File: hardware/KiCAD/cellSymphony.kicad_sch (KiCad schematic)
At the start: 11 parts, among them SW1 RotaryEncoder_Switch, SW2 RotaryEncoder_Switch, SW3 RotaryEncoder_Switch, SW4 RotaryEncoder_Switch, SW5 RotaryEncoder_Switch, U1 Raspberry Zero 2 W

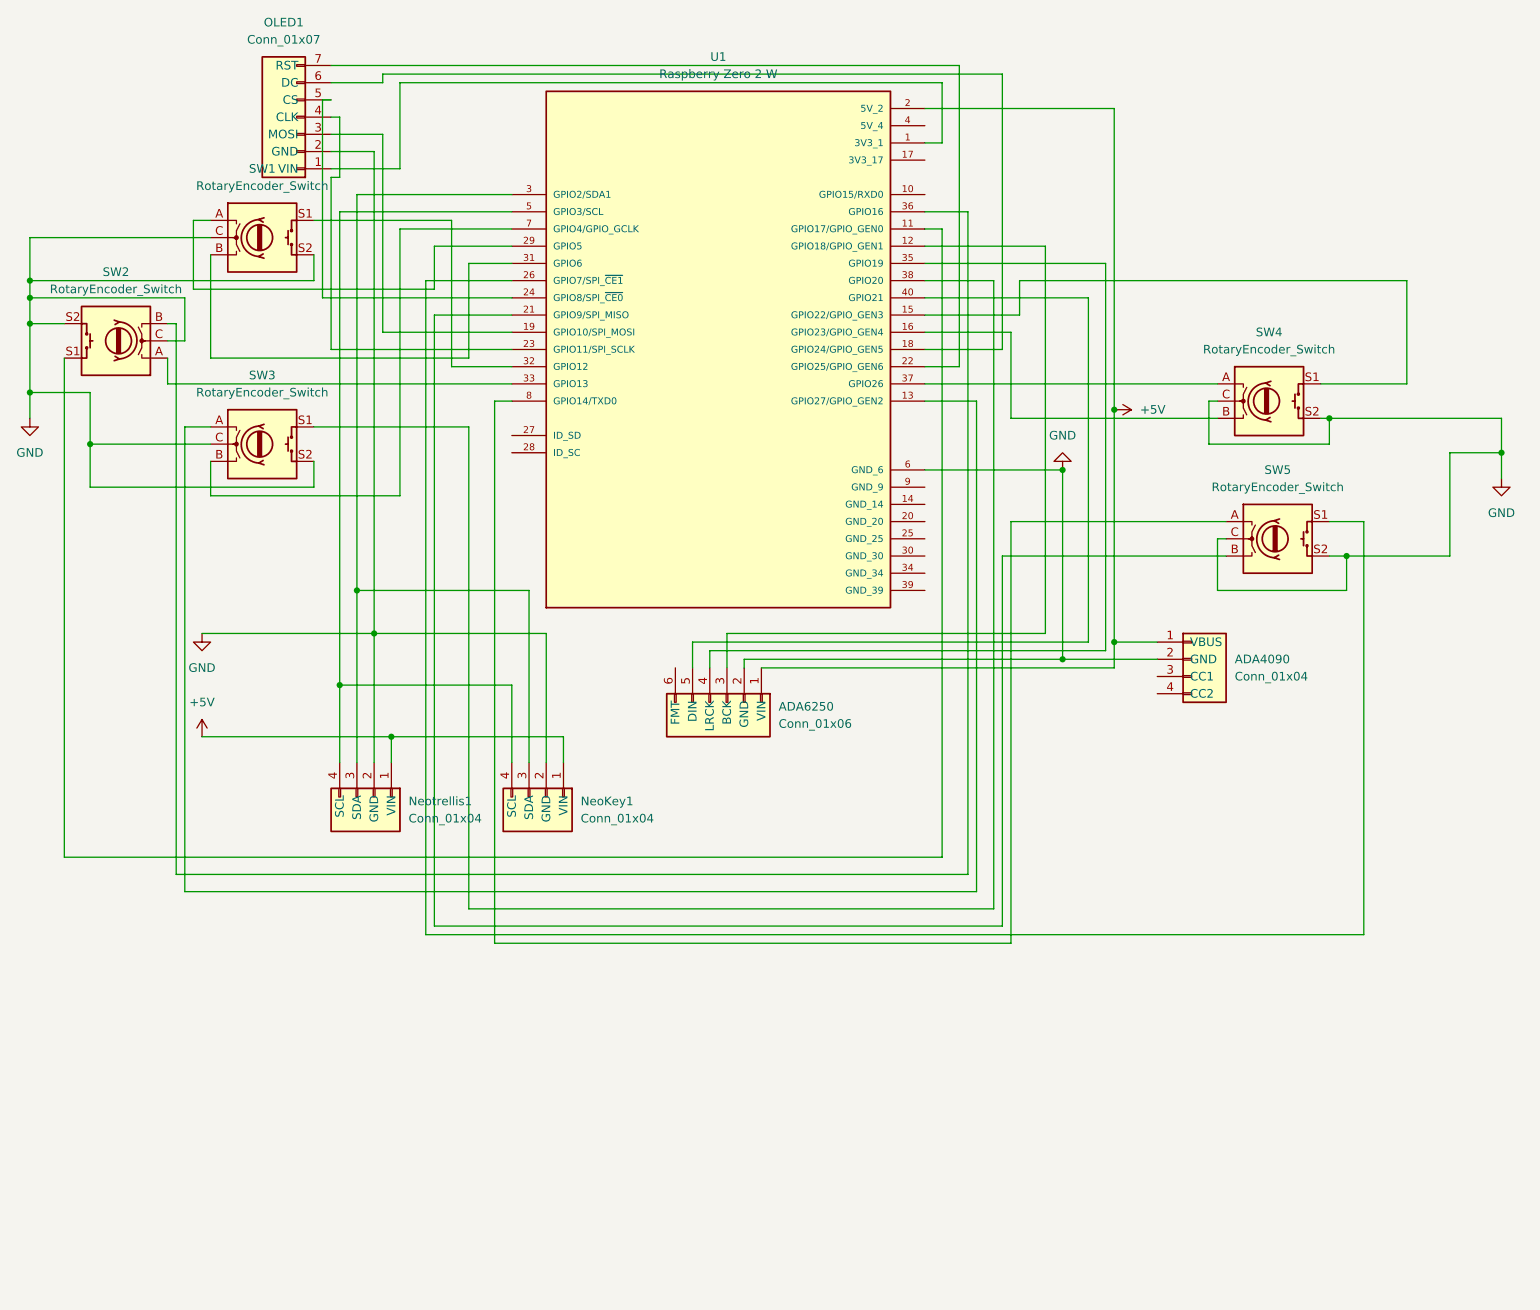
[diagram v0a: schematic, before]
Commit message: hardware: add new PCB revision with KiCAD libs and reports
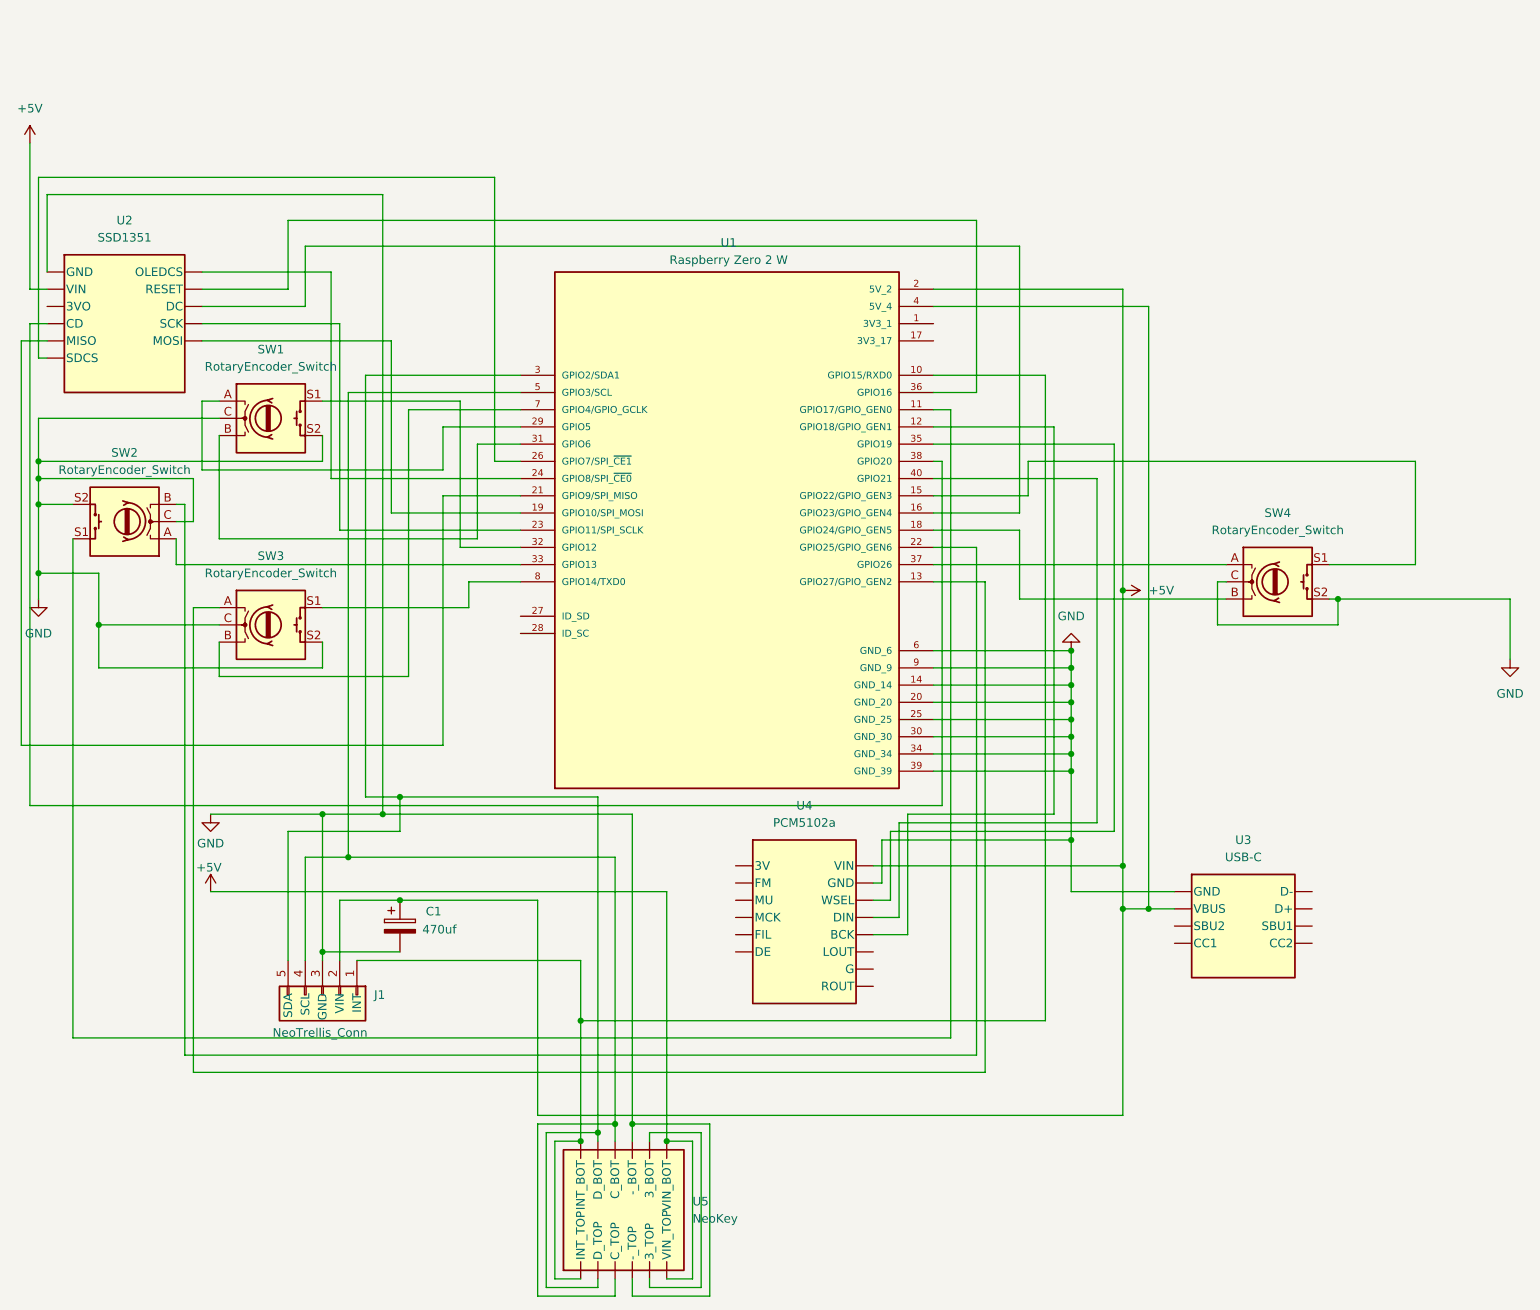
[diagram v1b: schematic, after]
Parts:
- removed ADA4090, NeoKey1, Neotrellis1: Conn_01x04, Connector_PinHeader_2.54mm:PinHeader_1x04_P2.54mm_Vertical, symbol Connector_Generic:Conn_01x04
- removed ADA6250: Conn_01x06, Connector_PinHeader_2.54mm:PinHeader_1x06_P2.54mm_Vertical, symbol Connector_Generic:Conn_01x07
- removed OLED1: Conn_01x07, Connector_PinHeader_2.54mm:PinHeader_1x07_P2.54mm_Vertical, symbol Connector_Generic:Conn_01x07
- removed SW5: RotaryEncoder_Switch, Rotary_Encoder:RotaryEncoder_Alps_EC11E-Switch_Vertical_H20mm, symbol Device:RotaryEncoder_Switch
- added C1: 470uf, Capacitor_THT:CP_Radial_D8.0mm_P3.50mm, symbol Device:C_Polarized
- added J1: NeoTrellis_Conn, adafruit-modules:Adafruit_NeoTrellis_Connector_1x5, symbol adafruit-modules:Adafruit_NeoTrellis_Connector_1x5
- added U2: SSD1351, adafruit-modules:Adafruit_SSD1351_OLED, symbol adafruit-modules:Adafruit_SSD1351_OLED
- added U3: USB-C, adafruit-modules:Adafruit_USB_C_Breakout, symbol adafruit-modules:Adafruit_USB_C_Breakout
- added U4: PCM5102a, adafruit-modules:Adafruit_PCM510x_I2S_DAC_6250, symbol adafruit-modules:Adafruit_PCM510x_I2S_DAC_6250
- added U5: NeoKey, adafruit-modules:Adafruit_NeoKey_1x4_QT, symbol adafruit-modules:Adafruit_NeoKey_1x4_QT
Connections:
- net +5V: now also U1.4 (5V_4), C1.1, J1.2 (VIN), U2.+ (VIN), U3.VBUS, U4.VIN, U5.VIN (VIN_BOT)
- net GND: now also U1.14 (GND_14), U1.20 (GND_20), U1.25 (GND_25), U1.30 (GND_30), U1.34 (GND_34), U1.39 (GND_39), U1.9 (GND_9), C1.2, J1.3 (GND), U2.G (GND), U3.GND, U4.GND, U5.- (-_BOT)
- net at SW3.S1: now also U1.8 (GPIO14/TXD0); no longer U1.38 (GPIO20)
- net at U1.3 (GPIO2/SDA1): now also J1.5 (SDA), U5.D (D_BOT)
- net at U1.5 (GPIO3/SCL): now also J1.4 (SCL), U5.C (C_BOT)
- net at U1.21 (GPIO9/SPI_MISO): now also U2.SO (MISO)
- net at U1.26 (GPIO7/SPI_~{CE1}): now also U2.SC (SDCS)
- net at U1.16 (GPIO23/GPIO_GEN4): now also U2.DC; no longer SW4.B
- net at U1.12 (GPIO18/GPIO_GEN1): now also U4.BCK
- net at U1.35 (GPIO19): now also U4.WSEL
- net at U1.40 (GPIO21): now also U4.DIN
- net at U1.36 (GPIO16): now also U2.R (RESET); no longer SW2.B
- net at U1.19 (GPIO10/SPI_MOSI): now also U2.SI (MOSI)
- net at U1.23 (GPIO11/SPI_SCLK): now also U2.CL (SCK)
- net at U1.24 (GPIO8/SPI_~{CE0}): now also U2.OC (OLEDCS)
- net at U1.18 (GPIO24/GPIO_GEN5): now also SW4.B
- net at U1.22 (GPIO25/GPIO_GEN6): now also SW2.B
- net at U1.10 (GPIO15/RXD0): now also J1.1 (INT), U5.INT (INT_BOT)
- new net: U1.38 (GPIO20), U2.CD
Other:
- moved on the sheet: SW1, SW2, SW3, SW4, U1
